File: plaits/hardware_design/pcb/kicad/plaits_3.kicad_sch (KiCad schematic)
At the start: 33 parts

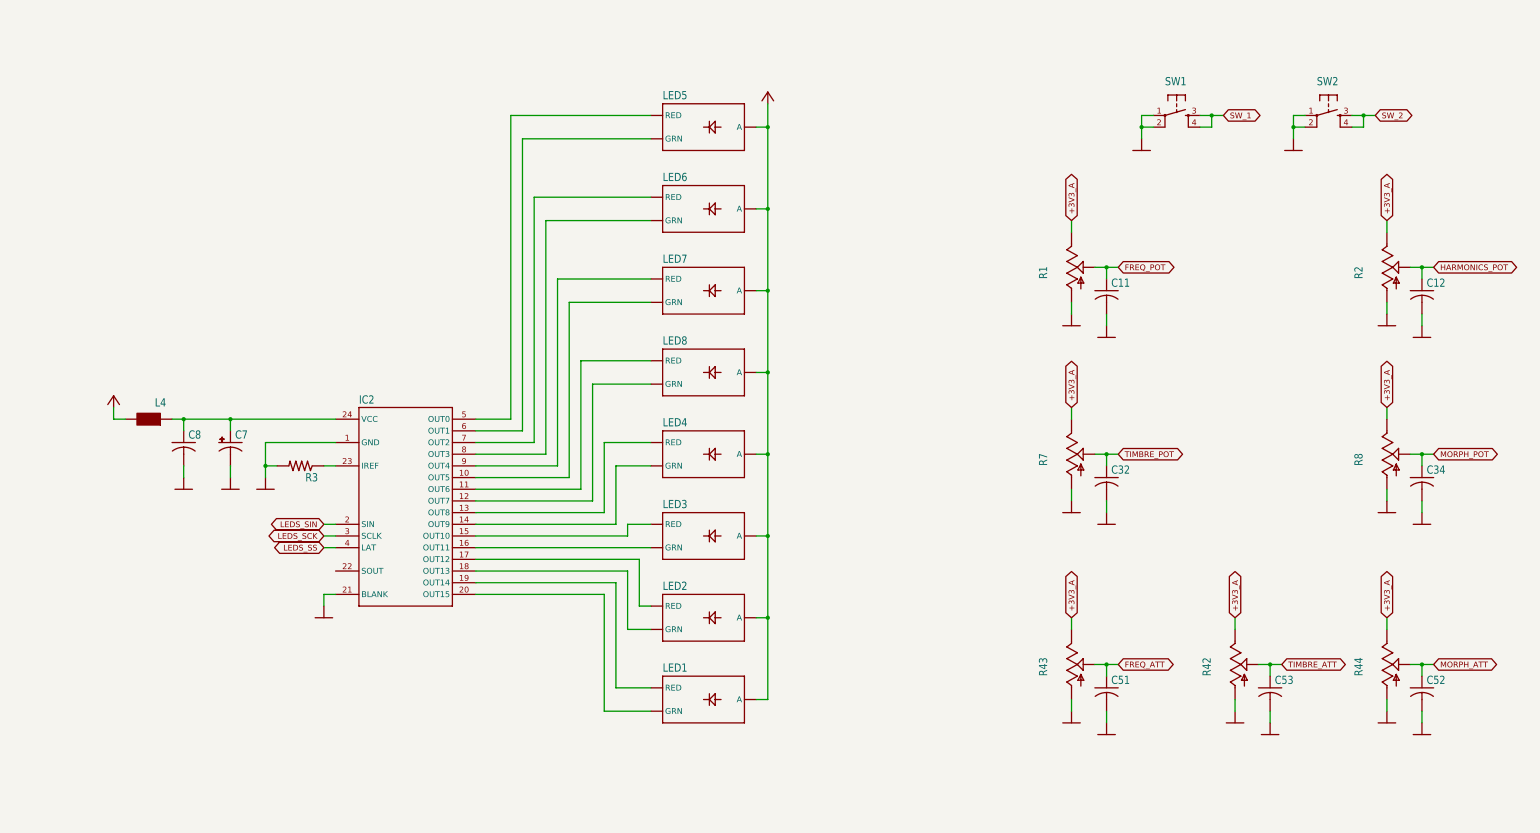
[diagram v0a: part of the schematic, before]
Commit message: plaits resized panasonic A -> B caps
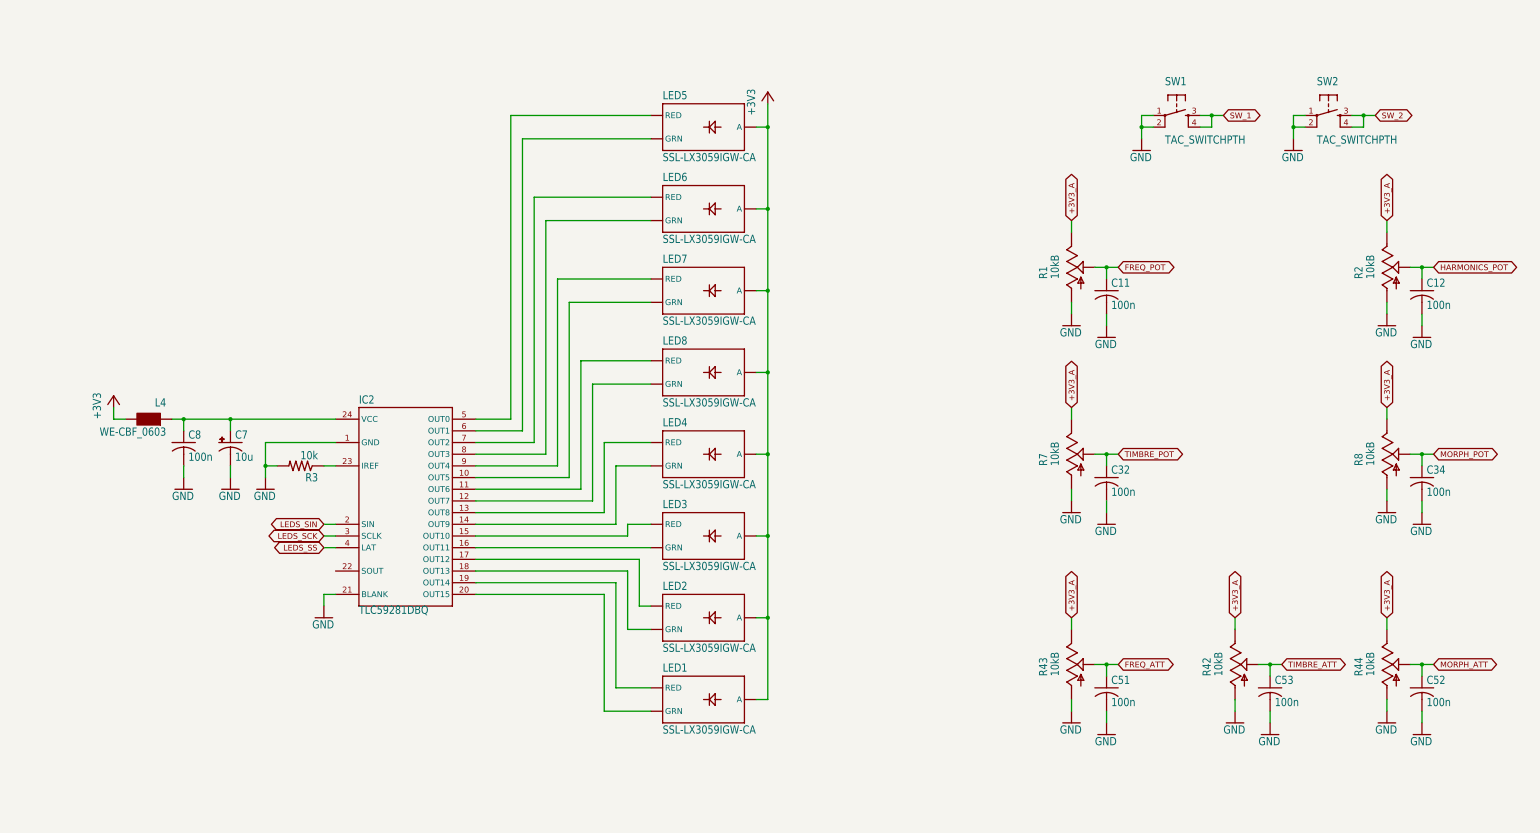
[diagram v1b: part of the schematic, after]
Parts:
- C11, C12, C32, C34, C51, C52, C53, C8: value (none) -> 100n; footprint (none) -> plaits:C0402
- C7: value (none) -> 10u; footprint (none) -> plaits:PANASONIC_B
- IC2: value (none) -> TLC59281DBQ; footprint (none) -> plaits:TSSOP24_0635
- JP1, JP2, JP3, JP4: value (none) -> FIDUCIAL1X2; footprint (none) -> plaits:FIDUCIAL-1X2
- L4: value (none) -> WE-CBF_0603; footprint (none) -> plaits:0603
- LED1, LED2, LED3, LED4, LED5, LED6, LED7, LED8: value (none) -> SSL-LX3059IGW-CA; footprint (none) -> plaits:LED-BICOLOR-THROUGHHOLE-LUMEX
- R1, R2, R7, R8: value (none) -> 10kB; footprint (none) -> plaits:ALPS_POT_VERTICAL_PS
- R3: value (none) -> 10k; footprint (none) -> plaits:R0402
- R42, R43, R44: value (none) -> 10kB; footprint (none) -> plaits:ALPS_POT_VERTICAL
- SW1, SW2: value (none) -> TAC_SWITCHPTH; footprint (none) -> plaits:TACTILE-PTH
